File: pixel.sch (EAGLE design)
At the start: 13 parts, among them IC1 STM32F030K6TX-LQFP32(7X7), Y1 8 MHz

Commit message: blah
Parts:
- removed Y1: 8 MHz, crystals:CRYSTAL_GROUNDED/SMD_3.2X2.5MM
- added C11: 0.1uF, rc:C-0603
- added C12: 100 nF, rc:C-0603
- added C13: 1nF, rc:C-1206
- added CON1, CON2: DS1066-07M-SIDE, pixel_masterlib:DS1066-07M-SIDE
- added D1: SMF05C, pixel_masterlib:SMF05C
- added D2: SMAJ12A, masterlib:SMAJ12A
- added IC2: ESDA6V1L, pixel_masterlib:ESDA6V1L
- added IC3: ST3485SOIC8, pixel_masterlib:ST3485SOIC8
- added IC4, IC5: MC74VHC1GT125, pixel_masterlib:MC74VHC1GT125
- added L1: 47UH, power_inductors:SDR0604-470KL
- added Q1: FDC6420C, pixel_masterlib:FDC6420C
- added R11, R12, R4, R5: 22R, rc:R-0805
- added R2, R3: 560R, rc:R-0603
- added R6: 10K, rc:R-0805
- added R9: 60R, rc:R-0603
- added RN1, RN2: 510R, pixel_masterlib:RESISTOR_ARRAY
- added SJ1, SJ2: (no value), eth_conv_master_lib:SOLDER_JOINT
- added Z1: 16MHz, watchdog_master_library:CRYSTAL-3.2X2.5-4P
- C1: value 4.7 uF -> 100 nF
- R1: value (none) -> 60R
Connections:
- net LED1_FB renamed RE/DE
- new net A: D2.P$1, IC2.C1, IC3.A, R1.2, R11.1, R11.2, R3.2
- new net B: D2.P$2, IC2.C2, IC3.B, R12.1, R12.2, R2.1, SJ2.1
- new net CLOCK_BUFFERED: IC4.OUT_Y, RN2.2
- new net DATA_IN: D1.D3, RN1.1
- new net DATA_OUT: RN2.1
- new net DE: IC3.!RE, IC3.DE
- new net LATCH_BUFFERED: IC5.OUT_Y, RN2.3
- new net N$10: R9.1, SJ2.2
- new net N$11: C13.1, SJ1.2
- new net N$12: CON2.6, RN2.6
- new net N$13: Q1B.G, R4.2
- new net N$14: R4.1
- new net N$15: Q1B.D, R5.1
- new net N$16: Q1A.D
- new net N$4: CON1.5, RN1.7
- new net N$5: CON1.6, RN1.6
- new net N$6: CON2.4, RN2.8
- new net N$7: Q1A.G, R5.2, R6.2
- new net N$8: R1.1, R9.2, SJ1.1
- new net N$9: CON2.5, RN2.7
- new net RS485_A: CON1.2, CON2.2
- new net RS485_B: CON1.3, CON2.3
- new net VDD_12V: Q1A.S, R6.1
- new net VDD_24V: CON1.1, CON2.1
- net CLOCK: now also D1.D4, IC4.IN_A, RN1.2
- net GND: now also C10.2, C11.1, C12.1, C13.2, CON1.7, CON2.7, D1.G, IC2.A, IC3.GND, IC4.GND, IC5.GND, Q1B.S, R3.1, Z1.GND; no longer C10.1, Y1.3
- net LATCH: now also D1.D5, IC5.IN_A, RN1.3
- net N$1: now also Z1.1; no longer Y1.2
- net N$2: now also CON1.4, RN1.8; no longer IC1.PF1, R1.1
- net N$3: now also C10.1, IC1.PF1, Z1.2; no longer C10.2, R1.2, Y1.1
- net RX: now also IC3.RO
- net TX: now also IC3.DI
- net VDD_3V3: now also C11.2, C12.2, IC3.VCC, IC4.VCC, IC5.VCC, R2.2
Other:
- note added: "INPUT"
- note added: "LED CHANNEL"
- note added: "Maybe should get rid of it"
- note added: "OUTPUT"
- note added: "R11 R12 may be replaced with 0-resistors"
- note added: "RS485"
- moved on the sheet: C1, C10, C2, C3, C4, C5, C6, C7, C8, C9, IC1, R1

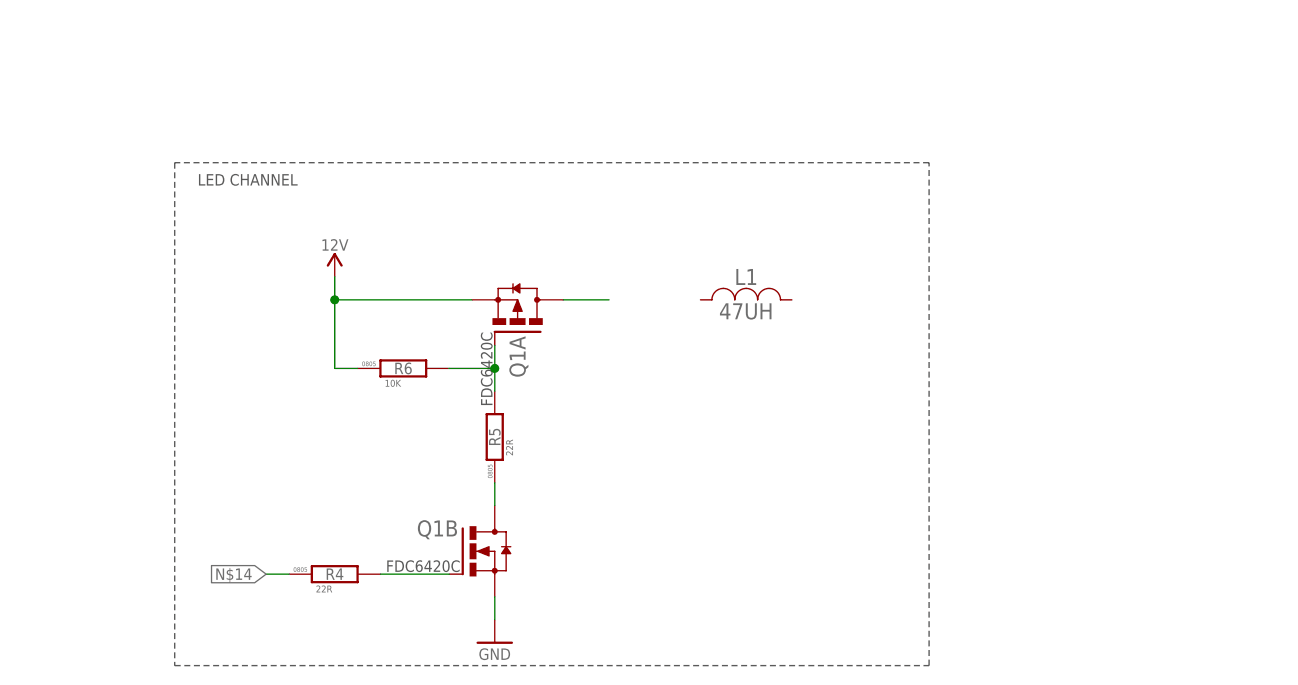
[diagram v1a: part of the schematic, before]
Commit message: Preliminary LED driver
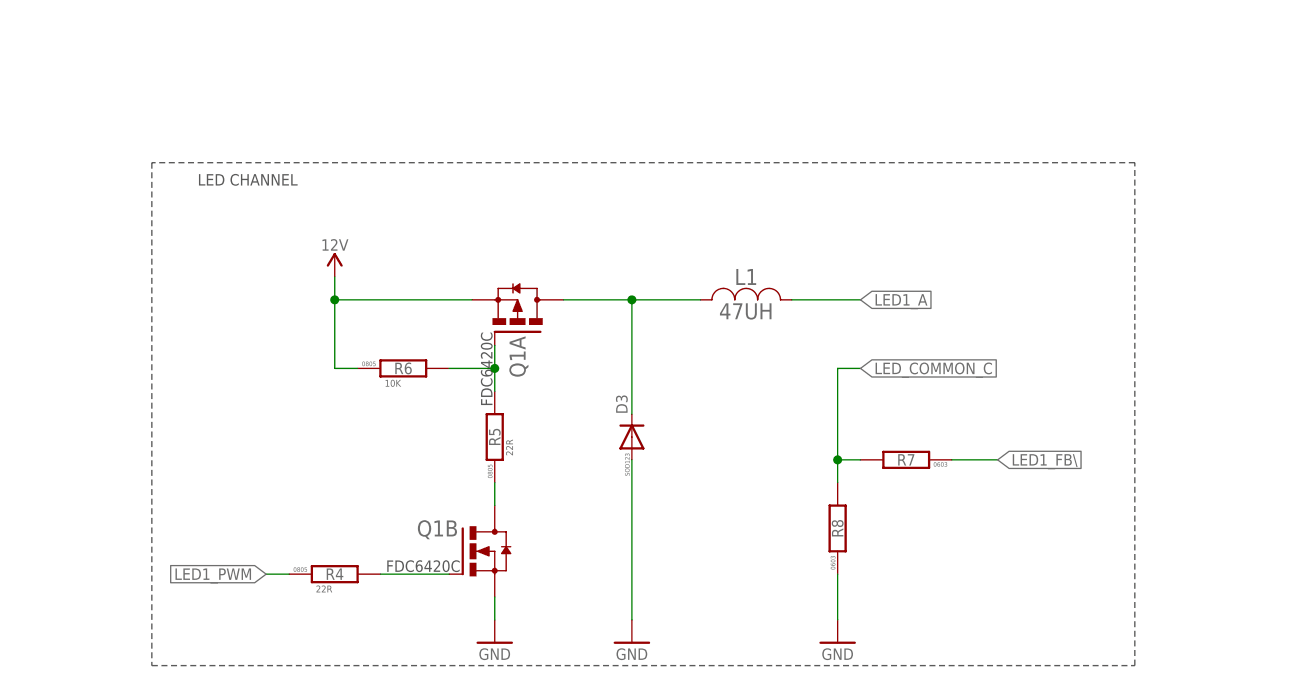
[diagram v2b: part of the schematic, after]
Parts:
- added D3: (no value), diodes:DIODE-SOD123
- added R7, R8: (no value), rc:R-0603
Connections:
- removed net N$14: R4.1
- removed net N$16: Q1A.D
- new net LED1_A: L1.2
- new net LED1_FB\: R7.1
- new net LED_COMMON_C: R7.2, R8.2
- new net N$17: D3.C, L1.1, Q1A.D
- net GND: now also D3.A, R8.1
- net LED1_PWM: now also R4.1
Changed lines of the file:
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@@
 <setting verticaltext="up"/>
 </settings>
-<grid distance="0.1" unitdist="inch" unit="inch" style="lines" multiple="1" display="no" altdistance="0.01" altunitdist="inch" altunit="inch"/>
+<grid distance="0.1" unitdist="inch" unit="inch" style="lines" multiple="1" display="yes" altdistance="0.01" altunitdist="inch" altunit="inch"/>
 <layers>
 <layer number="1" name="Top" color="4" fill="1" visible="no" active="no"/>
@@
 <part name="R5" library="rc" deviceset="R" device="-0805" value="22R"/>
 <part name="R6" library="rc" deviceset="R" device="-0805" value="10K"/>
+<part name="D3" library="diodes" deviceset="DIODE" device="-SOD123"/>
+<part name="GND23" library="supply_symbols" deviceset="GND" device="" value="GND"/>
+<part name="R7" library="rc" deviceset="R" device="-0603"/>
+<part name="R8" library="rc" deviceset="R" device="-0603"/>
+<part name="GND24" library="supply_symbols" deviceset="GND" device="" value="GND"/>
 </parts>
 <sheets>
@@
 <wire x1="281.94" y1="193.04" x2="223.52" y2="193.04" width="0.1524" layer="97" style="shortdash"/>
 <text x="226.06" y="195.58" size="2.54" layer="97">Maybe should get rid of it</text>
-<wire x1="38.1" y1="101.6" x2="38.1" y2="45.72" width="0.1524" layer="97" style="shortdash"/>
-<wire x1="38.1" y1="45.72" x2="121.92" y2="45.72" width="0.1524" layer="97" style="shortdash"/>
-<wire x1="121.92" y1="45.72" x2="121.92" y2="101.6" width="0.1524" layer="97" style="shortdash"/>
-<wire x1="121.92" y1="101.6" x2="38.1" y2="101.6" width="0.1524" layer="97" style="shortdash"/>
+<wire x1="35.56" y1="101.6" x2="35.56" y2="45.72" width="0.1524" layer="97" style="shortdash"/>
+<wire x1="35.56" y1="45.72" x2="144.78" y2="45.72" width="0.1524" layer="97" style="shortdash"/>
+<wire x1="144.78" y1="45.72" x2="144.78" y2="101.6" width="0.1524" layer="97" style="shortdash"/>
+<wire x1="144.78" y1="101.6" x2="35.56" y2="101.6" width="0.1524" layer="97" style="shortdash"/>
 <text x="40.64" y="99.06" size="1.27" layer="97">LED CHANNEL</text>
 </plain>
@@
 <instance part="R5" gate="G$1" x="73.66" y="71.12" rot="R90"/>
 <instance part="R6" gate="G$1" x="63.5" y="78.74"/>
+<instance part="D3" gate="G$1" x="88.9" y="71.12" rot="R90"/>
+<instance part="GND23" gate="1" x="88.9" y="48.26" rot="MR0"/>
+<instance part="R7" gate="G$1" x="119.38" y="68.58" rot="R180"/>
+<instance part="R8" gate="G$1" x="111.76" y="60.96" rot="R90"/>
+<instance part="GND24" gate="1" x="111.76" y="48.26" rot="MR0"/>
 </instances>
 <busses>
@@
 <wire x1="73.66" y1="50.8" x2="73.66" y2="53.34" width="0.1524" layer="91"/>
 </segment>
+<segment>
+<pinref part="GND23" gate="1" pin="GND"/>
+<pinref part="D3" gate="G$1" pin="A"/>
+<wire x1="88.9" y1="50.8" x2="88.9" y2="68.58" width="0.1524" layer="91"/>
+</segment>
+<segment>
+<pinref part="GND24" gate="1" pin="GND"/>
+<pinref part="R8" gate="G$1" pin="1"/>
+<wire x1="111.76" y1="50.8" x2="111.76" y2="55.88" width="0.1524" layer="91"/>
+</segment>
 </net>
 <net name="N$1" class="0">
@@
 <wire x1="106.68" y1="200.66" x2="109.22" y2="200.66" width="0.1524" layer="91"/>
 <label x="109.22" y="200.66" size="1.27" layer="95" rot="MR180" xref="yes"/>
+</segment>
+<segment>
+<pinref part="R4" gate="G$1" pin="1"/>
+<wire x1="50.8" y1="55.88" x2="48.26" y2="55.88" width="0.1524" layer="91"/>
+<label x="48.26" y="55.88" size="1.27" layer="95" rot="R180" xref="yes"/>
 </segment>
 </net>
@@
 </segment>
 </net>
-<net name="N$14" class="0">
-<segment>
-<pinref part="R4" gate="G$1" pin="1"/>
-<wire x1="50.8" y1="55.88" x2="48.26" y2="55.88" width="0.1524" layer="91"/>
-<label x="48.26" y="55.88" size="1.27" layer="95" rot="R180" xref="yes"/>
-</segment>
-</net>
 <net name="VDD_12V" class="0">
 <segment>
@@
 </segment>
 </net>
-<net name="N$16" class="0">
-<segment>
-<pinref part="Q1" gate="A" pin="D"/>
-<wire x1="81.28" y1="86.36" x2="86.36" y2="86.36" width="0.1524" layer="91"/>
-</segment>
-</net>
 <net name="N$7" class="0">
 <segment>
@@
 </segment>
 </net>
+<net name="N$17" class="0">
+<segment>
+<pinref part="D3" gate="G$1" pin="C"/>
+<wire x1="88.9" y1="86.36" x2="88.9" y2="73.66" width="0.1524" layer="91"/>
+<pinref part="Q1" gate="A" pin="D"/>
+<wire x1="81.28" y1="86.36" x2="88.9" y2="86.36" width="0.1524" layer="91"/>
+<pinref part="L1" gate="G$1" pin="1"/>
+<wire x1="88.9" y1="86.36" x2="96.52" y2="86.36" width="0.1524" layer="91"/>
+<junction x="88.9" y="86.36"/>
+</segment>
+</net>
+<net name="LED1_FB\" class="0">
+<segment>
+<label x="129.54" y="68.58" size="1.27" layer="95" xref="yes"/>
+<pinref part="R7" gate="G$1" pin="1"/>
+<wire x1="124.46" y1="68.58" x2="129.54" y2="68.58" width="0.1524" layer="91"/>
+</segment>
+</net>
+<net name="LED1_A" class="0">
+<segment>
+<pinref part="L1" gate="G$1" pin="2"/>
+<wire x1="106.68" y1="86.36" x2="114.3" y2="86.36" width="0.1524" layer="91"/>
+<label x="114.3" y="86.36" size="1.27" layer="95" xref="yes"/>
+</segment>
+</net>
+<net name="LED_COMMON_C" class="0">
+<segment>
+<pinref part="R8" gate="G$1" pin="2"/>
+<wire x1="111.76" y1="66.04" x2="111.76" y2="68.58" width="0.1524" layer="91"/>
+<pinref part="R7" gate="G$1" pin="2"/>
+<wire x1="111.76" y1="68.58" x2="114.3" y2="68.58" width="0.1524" layer="91"/>
+<wire x1="111.76" y1="68.58" x2="111.76" y2="78.74" width="0.1524" layer="91"/>
+<junction x="111.76" y="68.58"/>
+<wire x1="111.76" y1="78.74" x2="114.3" y2="78.74" width="0.1524" layer="91"/>
+<label x="114.3" y="78.74" size="1.27" layer="95" xref="yes"/>
+</segment>
+</net>

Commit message: minor changes
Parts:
- removed D3: (no value), diodes:DIODE-SOD123
- removed R8: (no value), rc:R-0603
- added C14: 10uF 6.3V, rc:C-1206
- added D4: CRS08-SOD123, eth_conv_master_lib:CRS08-SOD123
- added NRF24L01: NRF24L01, ali_modules:NRF24L01
- R7: value (none) -> 2R; device rc:R-0603 -> rc:R-R1206
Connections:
- removed net LED1_A: L1.2
- removed net LED1_FB\: R7.1
- removed net LED_COMMON_C: R7.2, R8.2
- new net MISO: IC1.PB4, NRF24L01.MISO
- new net MOSI: IC1.PB5, NRF24L01.MOSI
- new net NRF_CE: NRF24L01.CE
- new net NRF_CSN: NRF24L01.CSN
- new net NRF_IRQ: NRF24L01.IRQ
- new net SCK: IC1.PB3, NRF24L01.SCK
- net GND: now also C14.2, D4.A, NRF24L01.GND, R7.1; no longer D3.A, R8.1
- net N$17: now also D4.C; no longer D3.C
- net VDD_3V3: now also C14.1, NRF24L01.VCC
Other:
- note added: "OPTIONAL NRF24L01"
- note added: "R7 is 2 Ohms current shunt. So at 350mA voltage drop will be 0.7V. Power dissipation is 0.7*0.35 ~ 0.22W. 1206 resistors are 0.25W rated. Maybe should split it in 2 resistors"
- note added: "This part must be reworked to support COMMON ANODE LEDS"
- moved on the sheet: C10, C11, C13, C2, C3, C9, D2, IC2, IC3, L1, Q1A, Q1B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
